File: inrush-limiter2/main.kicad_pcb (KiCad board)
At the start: 2 copper layers, 32 parts, among them K1 RELAY_2RT, P1 CONN_01X04, P2 CONN_01X02, Q1 2N3904, Q2 PN2222A, T1 TRANSFO, U1 LM393, U2 50 ohm NTC

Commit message: improve traces
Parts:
- moved CP1 1.27 mm to (121.9, 76.2)
- moved RV1 1.27 mm to (118.1, 80.0)
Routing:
- net +5V: track 89.6 -> 84.2 mm
- net GND: track 248.3 -> 245.7 mm
- net Net-(R4-Pad2): track 17.6 -> 19.4 mm
- net Net-(CP1-Pad1): track 23.7 -> 22.4 mm
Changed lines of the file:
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@@
   (general
     (links 58)
-    (no_connects 5)
+    (no_connects 4)
     (area 110.105 9.824899 205.148001 96.28099)
     (thickness 1.6)
     (drawings 0)
-    (tracks 165)
+    (tracks 162)
     (zones 0)
     (modules 32)
@@
   )
   (module Capacitors_ThroughHole:C_Rect_L7_W3.5_P5 (layer F.Cu)
-    (at 120.65 76.2 270)
+    (at 121.92 76.2 270)
     (descr "Film Capacitor Length 7mm x Width 3.5mm, Pitch 5mm")
     (tags Capacitor)
@@
   )
   (module Potentiometers:Potentiometer_Bourns_3296W_3-8Zoll_Inline_ScrewUp (layer F.Cu)
-    (at 116.84 80.01)
+    (at 118.11 80.01)
     (descr "3296, 3/8, Square, Trimpot, Trimming, Potentiometer, Bourns")
     (tags "3296, 3/8, Square, Trimpot, Trimming, Potentiometer, Bourns")
@@
   (segment (start 142.24202 69.85) (end 142.24254 69.85052) (width 1) (layer B.Cu) (net 1) (status 30))
   (segment (start 138.43 69.84798) (end 138.43254 69.85052) (width 1) (layer B.Cu) (net 1) (status 30))
+  (segment (start 114.3 50.8) (end 114.3 93.98) (width 1) (layer B.Cu) (net 2))
+  (segment (start 114.3 93.98) (end 114.3 95.25) (width 1) (layer B.Cu) (net 2))
+  (segment (start 121.92 81.2) (end 121.92 81.28) (width 1) (layer B.Cu) (net 2) (status C00000))
+  (segment (start 121.92 81.28) (end 120.65 82.55) (width 1) (layer B.Cu) (net 2) (status 400000))
+  (segment (start 120.65 82.55) (end 120.65 85.09) (width 1) (layer B.Cu) (net 2) (status 800000))
   (segment (start 134.625 72.385) (end 132.085 72.385) (width 1) (layer B.Cu) (net 2))
-  (segment (start 130.82 71.12) (end 130.82 67.31) (width 1) (layer B.Cu) (net 2) (status 800000))
+  (segment (start 130.82 71.12) (end 130.82 67.31) (width 1) (layer B.Cu) (net 2))
   (segment (start 132.085 72.385) (end 130.82 71.12) (width 1) (layer B.Cu) (net 2))
   (segment (start 135.895 72.385) (end 134.625 72.385) (width 1) (layer B.Cu) (net 2))
@@
   (segment (start 121.92 67.31) (end 123.19 67.31) (width 1) (layer B.Cu) (net 2) (status 20))
   (segment (start 148.59052 54.60746) (end 148.59052 53.34052) (width 1) (layer B.Cu) (net 2) (status 10))
-  (segment (start 113.03 52.07) (end 113.03 95.25) (width 1) (layer B.Cu) (net 2))
-  (segment (start 114.3 50.8) (end 113.03 52.07) (width 1) (layer B.Cu) (net 2))
   (segment (start 146.05 50.8) (end 119.38 50.8) (width 1) (layer B.Cu) (net 2))
   (segment (start 119.38 50.8) (end 114.3 50.8) (width 1) (layer B.Cu) (net 2))
   (segment (start 148.59052 53.34052) (end 146.05 50.8) (width 1) (layer B.Cu) (net 2))
-  (segment (start 113.03 95.25) (end 114.3 95.25) (width 1) (layer B.Cu) (net 2))
   (segment (start 158.75 93.98) (end 158.75 87.63) (width 1) (layer B.Cu) (net 2))
   (segment (start 139.7 88.9) (end 137.16 88.9) (width 1) (layer B.Cu) (net 2) (status 20))
@@
   (segment (start 138.43 91.44) (end 137.16 91.44) (width 1) (layer B.Cu) (net 2) (status 20))
   (segment (start 125.73 95.25) (end 114.3 95.25) (width 1) (layer B.Cu) (net 2))
-  (segment (start 114.3 95.25) (end 113.03 95.25) (width 1) (layer B.Cu) (net 2))
   (segment (start 129.54 91.44) (end 129.54 95.25) (width 1) (layer B.Cu) (net 2) (status 10))
   (segment (start 125.73 95.25) (end 125.73 92.71) (width 1) (layer B.Cu) (net 2) (status 20))
@@
   (segment (start 148.59052 54.60746) (end 148.58746 54.60746) (width 1) (layer B.Cu) (net 2) (status 30))
   (segment (start 146.05 69.84694) (end 146.04746 69.84948) (width 1) (layer B.Cu) (net 2) (status 30))
-  (segment (start 120.73 81.2) (end 120.65 81.2) (width 1) (layer B.Cu) (net 2) (status 30))
-  (segment (start 120.65 81.2) (end 120.65 85.09) (width 1) (layer B.Cu) (net 2) (status 30))
+  (segment (start 122 81.2) (end 121.92 81.2) (width 1) (layer B.Cu) (net 2) (status 30))
   (segment (start 125.69 92.67) (end 125.73 92.71) (width 1) (layer B.Cu) (net 2) (status 30))
   (segment (start 123.19254 67.31052) (end 123.19 67.30798) (width 1) (layer B.Cu) (net 2) (status 30))
@@
   (segment (start 142.24 90.17) (end 142.24 92.71) (width 1) (layer B.Cu) (net 7) (status 10))
   (segment (start 142.24052 83.81948) (end 142.24 83.82) (width 1) (layer B.Cu) (net 7) (status 30))
-  (segment (start 116.84 71.12) (end 115.57 71.12) (width 1) (layer B.Cu) (net 8))
-  (segment (start 115.57 85.09) (end 116.84 85.09) (width 1) (layer B.Cu) (net 8))
-  (segment (start 114.3 83.82) (end 115.57 85.09) (width 1) (layer B.Cu) (net 8))
-  (segment (start 114.3 72.39) (end 114.3 83.82) (width 1) (layer B.Cu) (net 8))
-  (segment (start 115.57 71.12) (end 114.3 72.39) (width 1) (layer B.Cu) (net 8))
+  (segment (start 116.84 71.12) (end 115.57 72.39) (width 1) (layer B.Cu) (net 8) (status 400000))
+  (segment (start 115.57 83.82) (end 116.84 85.09) (width 1) (layer B.Cu) (net 8) (status 800000))
+  (segment (start 115.57 72.39) (end 115.57 83.82) (width 1) (layer B.Cu) (net 8))
+  (segment (start 118.11 74.93) (end 118.11 72.39) (width 1) (layer B.Cu) (net 8) (status 400000))
+  (segment (start 118.11 72.39) (end 116.84 71.12) (width 1) (layer B.Cu) (net 8) (status 800000))
   (segment (start 170.18 76.2) (end 163.83 76.2) (width 2.5) (layer B.Cu) (net 9) (status 30))
   (segment (start 186.69 36.83) (end 186.52998 35.39998) (width 0.75) (layer B.Cu) (net 11) (status 30))
@@
   (segment (start 125.73 85.09) (end 125.73 81.28) (width 1) (layer B.Cu) (net 19) (status 30))
   (segment (start 120.65 92.71) (end 116.84 92.71) (width 1) (layer B.Cu) (net 20) (status 30))
-  (segment (start 120.65 76.2) (end 118.11 76.2) (width 1) (layer B.Cu) (net 21))
-  (segment (start 118.11 76.2) (end 116.84 77.47) (width 1) (layer B.Cu) (net 21))
+  (segment (start 121.92 76.2) (end 120.65 76.2) (width 1) (layer B.Cu) (net 21) (status 400000))
+  (segment (start 119.38 77.47) (end 118.11 77.47) (width 1) (layer B.Cu) (net 21) (status 800000))
+  (segment (start 120.65 76.2) (end 119.38 77.47) (width 1) (layer B.Cu) (net 21))
   (segment (start 123.19 77.47) (end 123.19 86.36) (width 1) (layer B.Cu) (net 21))
   (segment (start 121.92 76.2) (end 123.19 77.47) (width 1) (layer B.Cu) (net 21))
   (segment (start 125.73 88.9) (end 129.54 88.9) (width 1) (layer B.Cu) (net 21) (status 20))
   (segment (start 123.19 86.36) (end 125.73 88.9) (width 1) (layer B.Cu) (net 21))
-  (segment (start 121.92 76.2) (end 120.65 76.2) (width 1) (layer B.Cu) (net 21) (status 20))
-  (segment (start 132.08 76.2) (end 132.08 78.74) (width 1) (layer B.Cu) (net 22) (status 400000))
+  (segment (start 121.92 76.2) (end 121.92 76.2) (width 1) (layer B.Cu) (net 21) (status 20))
+  (segment (start 116.84 63.5) (end 116.84 59.69) (width 1) (layer B.Cu) (net 22) (status C00000))
+  (segment (start 116.84 59.69) (end 116.84 55.88) (width 1) (layer B.Cu) (net 22) (status C00000))
+  (segment (start 132.08 76.2) (end 132.08 78.74) (width 1) (layer B.Cu) (net 22))
   (segment (start 129.54 78.74) (end 130.81 78.74) (width 1) (layer B.Cu) (net 22))
   (segment (start 125.73 73.66) (end 125.73 76.2) (width 1) (layer B.Cu) (net 22))
@@
   (segment (start 132.08 78.74) (end 137.16 78.74) (width 1) (layer B.Cu) (net 22))
   (segment (start 116.84 63.5) (end 116.84 67.31) (width 1) (layer B.Cu) (net 22) (status 10))
-  (segment (start 116.84 59.69) (end 114.3 59.69) (width 1) (layer B.Cu) (net 22) (status 10))
-  (segment (start 116.84 55.88) (end 115.57 55.88) (width 1) (layer B.Cu) (net 22) (status 10))
-  (segment (start 114.3 60.96) (end 116.84 63.5) (width 1) (layer B.Cu) (net 22) (status 20))
-  (segment (start 114.3 57.15) (end 114.3 59.69) (width 1) (layer B.Cu) (net 22))
-  (segment (start 114.3 59.69) (end 114.3 60.96) (width 1) (layer B.Cu) (net 22))
-  (segment (start 115.57 55.88) (end 114.3 57.15) (width 1) (layer B.Cu) (net 22))
   (segment (start 116.84 67.31) (end 125.73 76.2) (width 1) (layer B.Cu) (net 22))
   (segment (start 147.32 76.2) (end 149.86 76.2) (width 1) (layer B.Cu) (net 22) (status 10))

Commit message: update
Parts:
- moved R2 2.84 mm to (127.0, 71.1)
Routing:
- net +5V: track 84.2 -> 78.8 mm
- net Net-(R2-Pad2): track 8.15 -> 11.2 mm
- net Net-(CP1-Pad1): track 22.4 -> 24.2 mm
- net Net-(D2-Pad2): track 5.08 -> 3.81 mm
- net GND: track 245.7 -> 246.5 mm

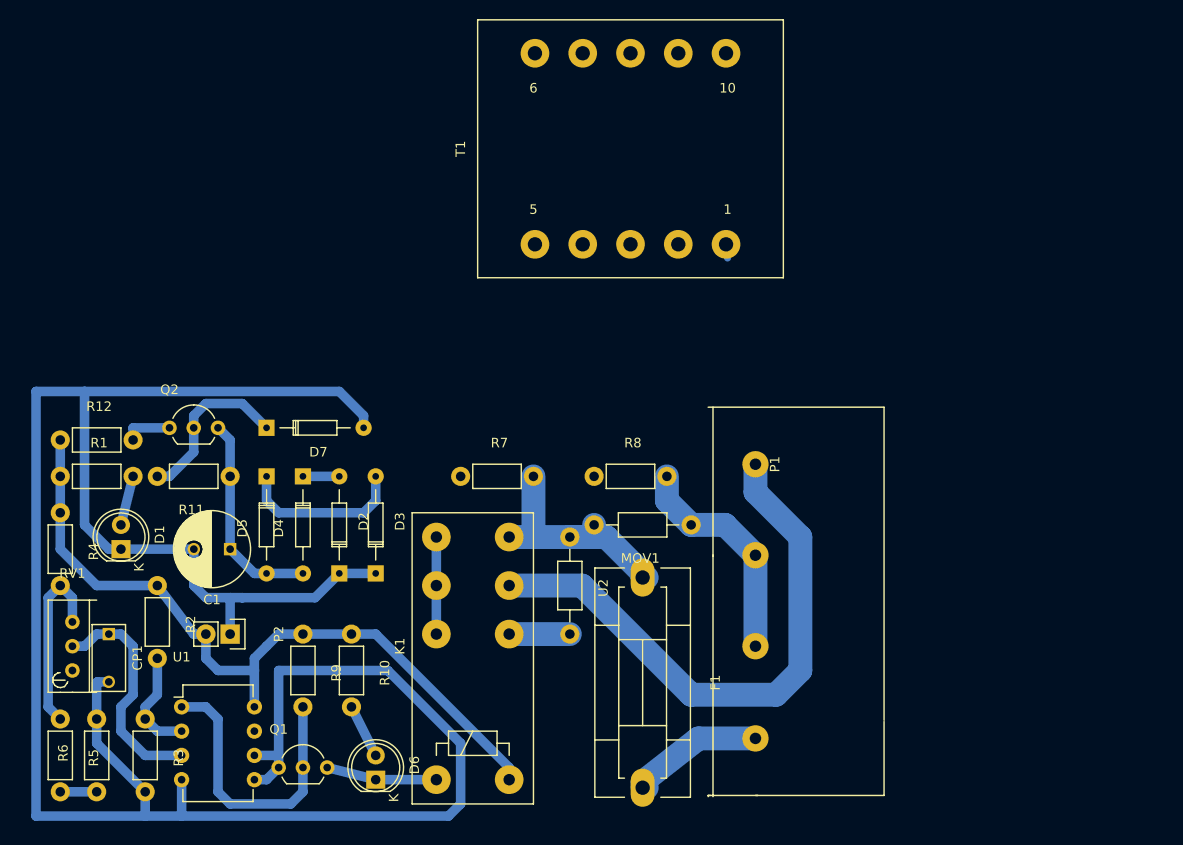
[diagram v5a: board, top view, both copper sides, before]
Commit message: add new transformer schematic and footprint
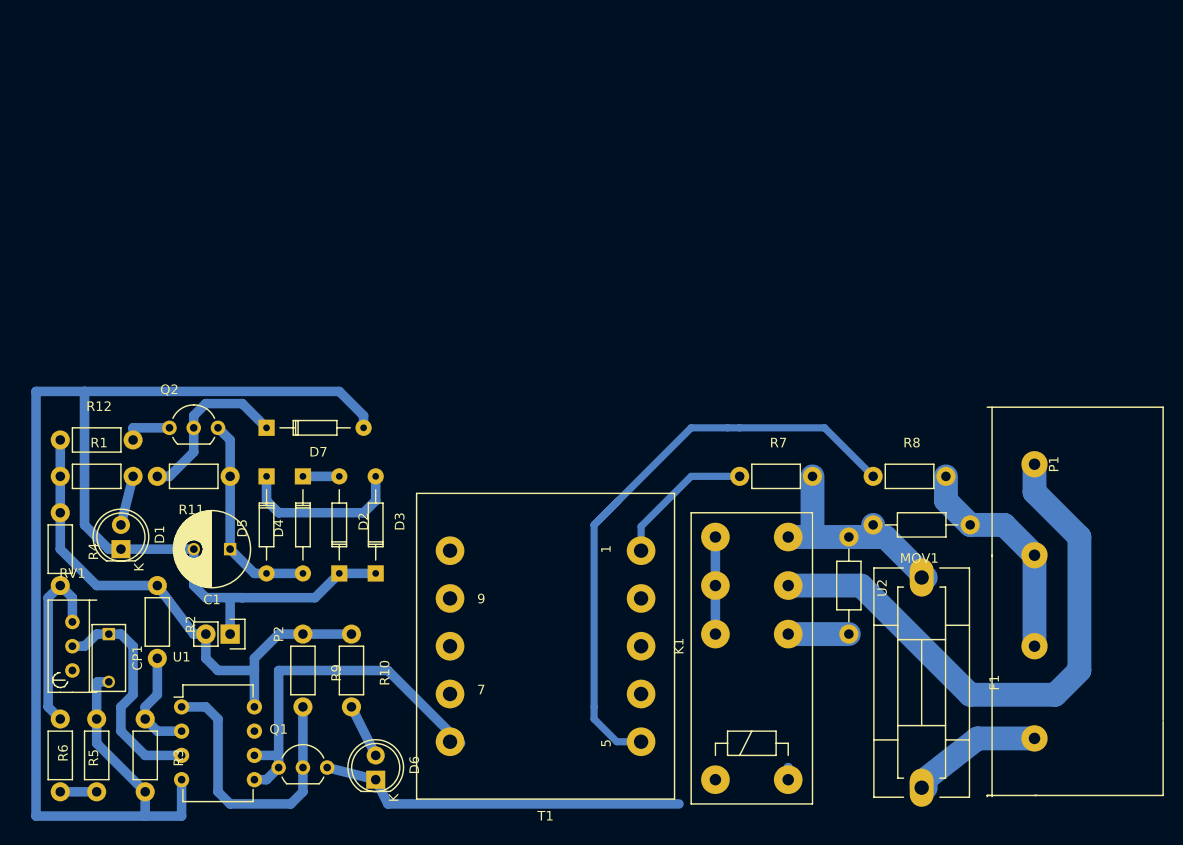
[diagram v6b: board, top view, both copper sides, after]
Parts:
- T1: value TRANSFO -> MY-TRANSFO; footprint Transformers_CHK:Trafo_CHK-EI30-2VA_Neutral -> test:my-transformer
- moved T1 52.8 mm to (167.6, 77.5), turned to 180 degrees
- moved MOV1 29.2 mm to (212.1, 64.8)
- moved R7 29.2 mm to (188.0, 59.7)
- moved R8 29.2 mm to (201.9, 59.7)
- moved F1 29.2 mm to (207.0, 81.3)
- moved K1 29.2 mm to (193.0, 91.4)
- moved P1 29.2 mm to (224.8, 61.0)
- moved U2 29.2 mm to (199.4, 66.0)
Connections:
- T1 pad 2: AC-neut-low -> (no net)
- T1 pad 3: Net-(D3-Pad2) -> (no net)
- T1 pad 4: Net-(D2-Pad2) -> (no net)
- T1 pad 5: (no net) -> AC-neut-low
- T1 pad 7: (no net) -> Net-(D3-Pad2)
- T1 pad 9: (no net) -> Net-(D2-Pad2)
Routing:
- net AC-neut-low: track 0.00 -> 65.3 mm
- net GND: track 246.5 -> 210.4 mm
- net Net-(D6-Pad1): track 12.9 -> 38.6 mm
- net +5V: track 78.8 -> 56.5 mm
- net AC-live-f-low: track 1.44 -> 15.0 mm

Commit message: tidying
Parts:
- moved R8 17.3 mm to (185.4, 54.6)
- moved MOV1 11.7 mm to (204.5, 55.9), turned to 270 degrees
- moved T1 8.89 mm to (167.6, 68.6)
- moved R7 2.54 mm to (185.4, 59.7)
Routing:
- net +5V: track 56.5 -> 113.7 mm
- net GND: track 210.4 -> 179.3 mm
- net AC-neut-low: track 65.3 -> 40.0 mm
- net AC-neut: track 23.7 -> 42.8 mm
- net Net-(D2-Pad2): track 3.81 -> 21.4 mm
- net Net-(D3-Pad2): track 17.6 -> 34.2 mm
- net AC-live-f-low: track 15.0 -> 8.24 mm
- net Net-(D6-Pad1): track 38.6 -> 40.8 mm
- net AC-live-f: track 27.0 -> 25.7 mm

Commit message: more tidying
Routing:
- net GND: track 179.3 -> 172.4 mm
- net Net-(R4-Pad2): track 19.4 -> 15.5 mm
- net AC-live-f: track 25.7 -> 23.2 mm
- net +5V: track 113.7 -> 112.5 mm
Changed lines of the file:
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@@
   (general
     (links 58)
-    (no_connects 2)
+    (no_connects 4)
     (area 110.105 47.685 234.358001 96.28099)
     (thickness 1.6)
     (drawings 0)
-    (tracks 184)
+    (tracks 175)
     (zones 0)
     (modules 32)
@@
   (segment (start 119.38 50.8) (end 114.3 50.8) (width 1) (layer B.Cu) (net 2))
   (segment (start 148.59052 53.34052) (end 146.05 50.8) (width 1) (layer B.Cu) (net 2))
-  (segment (start 139.7 88.9) (end 137.16 88.9) (width 1) (layer B.Cu) (net 2) (status 20))
-  (segment (start 139.7 90.17) (end 138.43 91.44) (width 1) (layer B.Cu) (net 2) (status 10))
-  (segment (start 138.43 91.44) (end 137.16 91.44) (width 1) (layer B.Cu) (net 2) (status 20))
   (segment (start 125.73 95.25) (end 114.3 95.25) (width 1) (layer B.Cu) (net 2))
   (segment (start 129.54 91.44) (end 129.54 95.25) (width 1) (layer B.Cu) (net 2) (status 10))
   (segment (start 125.73 95.25) (end 125.73 92.71) (width 1) (layer B.Cu) (net 2) (status 20))
   (segment (start 129.54 95.25) (end 125.73 95.25) (width 1) (layer B.Cu) (net 2))
-  (segment (start 139.7 88.9) (end 139.7 90.17) (width 1) (layer B.Cu) (net 2) (status 20))
   (segment (start 139.69746 90.17254) (end 139.7 90.17) (width 1) (layer B.Cu) (net 2) (status 30))
   (segment (start 146.04746 69.84948) (end 146.04746 69.85254) (width 1) (layer B.Cu) (net 2) (status 30))
@@
   (segment (start 207.01 69.85) (end 203.2 66.04) (width 2.5) (layer B.Cu) (net 3) (status 10))
   (segment (start 203.2 66.04) (end 199.39 66.04) (width 2.5) (layer B.Cu) (net 3) (status 20))
-  (segment (start 201.93 66.04) (end 199.39 66.04) (width 2.5) (layer B.Cu) (net 3) (status 20))
   (segment (start 207.01 70.27926) (end 207.01 69.85) (width 2.5) (layer B.Cu) (net 3) (status 30))
   (segment (start 199.39 66.04) (end 193.04 66.04) (width 2.5) (layer B.Cu) (net 3) (status 30))
@@
   (segment (start 142.24254 59.69052) (end 146.04642 59.69052) (width 1) (layer B.Cu) (net 4) (status 30))
   (segment (start 146.04642 59.69052) (end 146.04746 59.68948) (width 1) (layer B.Cu) (net 4) (status 30))
-  (segment (start 218.821 58.42) (end 218.821 58.801) (width 2.5) (layer B.Cu) (net 5) (status C00000))
-  (segment (start 218.821 58.801) (end 223.52 63.5) (width 2.5) (layer B.Cu) (net 5) (status 400000))
-  (segment (start 223.52 63.5) (end 223.52 66.04) (width 2.5) (layer B.Cu) (net 5))
+  (segment (start 218.821 58.42) (end 218.821 58.801) (width 2.5) (layer B.Cu) (net 5) (status 30))
+  (segment (start 218.821 58.801) (end 223.52 63.5) (width 2.5) (layer B.Cu) (net 5) (status 10))
+  (segment (start 223.52 63.5) (end 223.52 80.01) (width 2.5) (layer B.Cu) (net 5))
   (segment (start 220.98 82.55) (end 212.09 82.55) (width 2.5) (layer B.Cu) (net 5))
-  (segment (start 223.52 66.04) (end 223.52 80.01) (width 2.5) (layer B.Cu) (net 5))
   (segment (start 223.52 80.01) (end 220.98 82.55) (width 2.5) (layer B.Cu) (net 5))
   (segment (start 200.66 71.12) (end 193.04 71.12) (width 2.5) (layer B.Cu) (net 5) (status 20))
   (segment (start 212.09 82.55) (end 200.66 71.12) (width 2.5) (layer B.Cu) (net 5))
-  (segment (start 218.821 67.945) (end 218.821 67.691) (width 2.5) (layer B.Cu) (net 6) (status C00000))
-  (segment (start 218.821 67.691) (end 205.74 54.61) (width 2.5) (layer B.Cu) (net 6) (status 400000))
+  (segment (start 218.821 67.945) (end 218.821 67.691) (width 2.5) (layer B.Cu) (net 6) (status 30))
+  (segment (start 218.821 67.691) (end 205.74 54.61) (width 2.5) (layer B.Cu) (net 6) (status 10))
   (segment (start 205.74 54.61) (end 203.2 54.61) (width 2.5) (layer B.Cu) (net 6))
-  (segment (start 204.47 55.88) (end 203.2 54.61) (width 2.5) (layer B.Cu) (net 6))
-  (segment (start 203.2 54.61) (end 193.04 54.61) (width 2.5) (layer B.Cu) (net 6))
+  (segment (start 204.47 55.88) (end 203.2 54.61) (width 2.5) (layer B.Cu) (net 6) (status 10))
+  (segment (start 203.2 54.61) (end 193.04 54.61) (width 2.5) (layer B.Cu) (net 6) (status 20))
   (segment (start 218.821 77.47) (end 218.821 67.945) (width 2.5) (layer B.Cu) (net 6) (status 30))
   (segment (start 142.24 83.82) (end 142.24 90.17) (width 1) (layer B.Cu) (net 7) (status 30))
@@
   (segment (start 142.24 90.17) (end 142.24 92.71) (width 1) (layer B.Cu) (net 7) (status 10))
   (segment (start 142.24052 83.81948) (end 142.24 83.82) (width 1) (layer B.Cu) (net 7) (status 30))
-  (segment (start 116.84 71.12) (end 115.57 72.39) (width 1) (layer B.Cu) (net 8) (status 10))
-  (segment (start 115.57 83.82) (end 116.84 85.09) (width 1) (layer B.Cu) (net 8) (status 20))
-  (segment (start 115.57 72.39) (end 115.57 83.82) (width 1) (layer B.Cu) (net 8))
+  (segment (start 116.205 76.835) (end 116.205 84.455) (width 1) (layer B.Cu) (net 8) (status 20))
+  (segment (start 116.205 84.455) (end 116.84 85.09) (width 1) (layer B.Cu) (net 8) (status 30))
+  (segment (start 118.11 74.93) (end 116.205 76.835) (width 1) (layer B.Cu) (net 8) (status 10))
   (segment (start 118.11 74.93) (end 118.11 72.39) (width 1) (layer B.Cu) (net 8) (status 10))
   (segment (start 118.11 72.39) (end 116.84 71.12) (width 1) (layer B.Cu) (net 8) (status 20))
@@
   (segment (start 119.38 77.47) (end 118.11 77.47) (width 1) (layer B.Cu) (net 21) (status 20))
   (segment (start 120.65 76.2) (end 119.38 77.47) (width 1) (layer B.Cu) (net 21))
-  (segment (start 154.94 87.63) (end 152.4 85.09) (width 1) (layer B.Cu) (net 22))
+  (segment (start 193.04 91.44) (end 190.5 88.9) (width 1) (layer B.Cu) (net 22) (status 10))
+  (segment (start 152.4 86.36) (end 152.4 77.47) (width 1) (layer B.Cu) (net 22))
+  (segment (start 154.94 88.9) (end 152.4 86.36) (width 1) (layer B.Cu) (net 22))
+  (segment (start 190.5 88.9) (end 154.94 88.9) (width 1) (layer B.Cu) (net 22))
   (segment (start 152.4 77.47) (end 151.13 76.2) (width 1) (layer B.Cu) (net 22))
-  (segment (start 151.13 76.2) (end 149.86 76.2) (width 1) (layer B.Cu) (net 22))
-  (segment (start 149.86 76.2) (end 147.32 76.2) (width 1) (layer B.Cu) (net 22) (status 10))
-  (segment (start 152.4 77.47) (end 152.4 85.09) (width 1) (layer B.Cu) (net 22))
-  (segment (start 154.94 87.63) (end 190.5 87.63) (width 1) (layer B.Cu) (net 22))
-  (segment (start 190.5 87.63) (end 193.04 90.17) (width 1) (layer B.Cu) (net 22) (status 800000))
-  (segment (start 193.04 90.17) (end 193.04 91.44) (width 1) (layer B.Cu) (net 22) (status C00000))
-  (segment (start 193.04 91.44) (end 191.77 91.44) (width 1) (layer B.Cu) (net 22) (status 30))
+  (segment (start 151.13 76.2) (end 147.32 76.2) (width 1) (layer B.Cu) (net 22) (status 20))
   (segment (start 127 71.12) (end 120.65 71.12) (width 1) (layer B.Cu) (net 22) (status 10))
   (segment (start 116.84 67.31) (end 116.84 63.5) (width 1) (layer B.Cu) (net 22) (status 20))
